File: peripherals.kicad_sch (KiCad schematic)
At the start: 25 parts, among them J10 0533980471, J14 SM04B-SRSS-TB-LF-SN, J7 200528-0100, J8 200528-0100, U33 NTS0102, U35 AP22653, U9 SN74AXC4T774

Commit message: v2.0 Schematic updates
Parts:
- removed C108: 100nF, Capacitor_SMD:C_0603_1608Metric, symbol Device:C_Small
- removed D17, D18: TPD1E0B04, Diode_SMD:D_SOD-882, symbol Device:D_TVS_Small
- removed J14: SM04B-SRSS-TB-LF-SN, JetsonCarrier:Conn_JST_SH_1x4_SM04B-SRSS-TB-LF-SN, symbol JetsonCarrier:JST_SH_1x4_SM04B-SRSS-TB-LF-SN
- removed R145: 10k, Resistor_SMD:R_0603_1608Metric, symbol Device:R_Small
- removed R146: 100k, Resistor_SMD:R_0603_1608Metric, symbol Device:R_Small
- removed R147: 15k, Resistor_SMD:R_0603_1608Metric, symbol Device:R_Small
- removed RN3: 4x0R, Resistor_SMD:R_Array_Concave_4x0402, symbol Device:R_Pack04
- removed TP2, TP3: TP_0.75mm_SMD, JetsonCarrier:TP_SMD_0.75mm, symbol Connector:TestPoint
- removed U35: AP22653, JetsonCarrier:DFN-6-1EP_2x2mm_P0.65mm_EP1x1.6mm, symbol JetsonCarrier:AP22653
- removed U9: SN74AXC4T774, Package_DFN_QFN:UQFN-16_1.8x2.6mm_P0.4mm, symbol JetsonCarrier:SN74AXC4T774
- added U9: NTS0102, JetsonCarrier:XSON-8_1x1.95mm_P0.5mm, symbol JetsonCarrier:NTS0102
- C40, C41: Dielectric (none) -> X5R; MPN C1005X6S1A105K050BC -> GRM155R61H104KE14D; Manufacturer TDK -> Murata; Voltage (none) -> 50V
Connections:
- net MB_CS is gone; now on net GND: J8.6 (Pin_6)
- net MB_MISO is gone; now on net GND: J8.9 (Pin_9)
- net +1V8: now also C40.1, U9.3 (VCC_{A}), U9.6 (OE); no longer C41.1
- net GND: now also C40.2, J8.4 (Pin_4), U9.2 (GND); no longer C40.1, J8.5 (Pin_5)
- net JETSON_EN: now also J8.5 (Pin_5); no longer J8.4 (Pin_4)
- net MB_3V3: now also C41.1, U9.7 (VCC_{B}); no longer C40.2
- net UART1_RXD: now also U9.5 (A_{1})
- net UART1_TXD: now also U9.4 (A_{2})
- net MB_MOSI renamed MB_JETSON_RX
- net MB_JETSON_RX: now also U9.8 (B_{1})
- net MB_SCK renamed MB_JETSON_TX
- net MB_JETSON_TX: now also U9.1 (B_{2})
- no-connect marks 5 -> 0
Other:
- note added: "Mainboard FPC Connector"
- note added: "USB 2.0 FPC Connector"
- note removed: "I2C connector"
- company: Argus-1 Cubesat -> Carnegie Mellon University
- title: Jetson Carrier Board -> Argus Carrierboard
- moved on the sheet: C12, C33, C44, C48, J10, J7, J8, TP29, TP30, TP31, U33

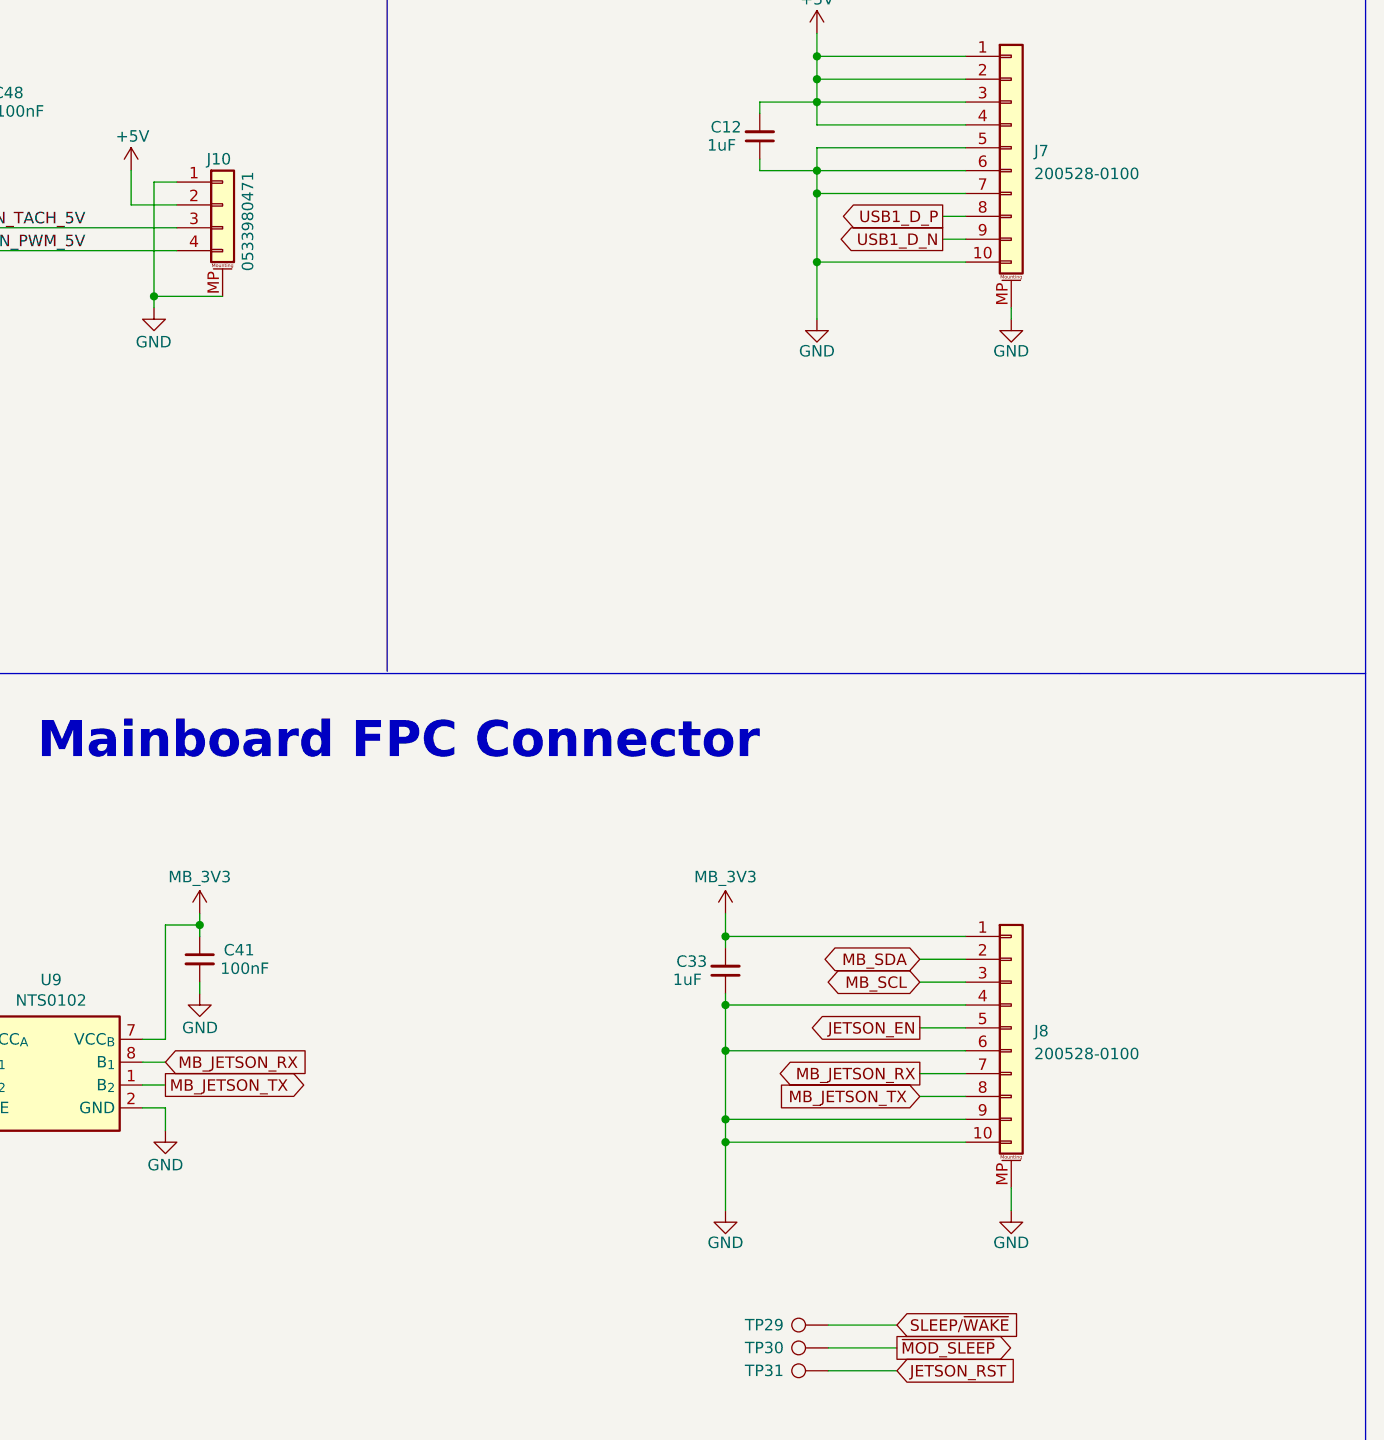
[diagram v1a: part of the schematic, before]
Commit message: v2.0 Layout completed. Exported BOM and STEP files
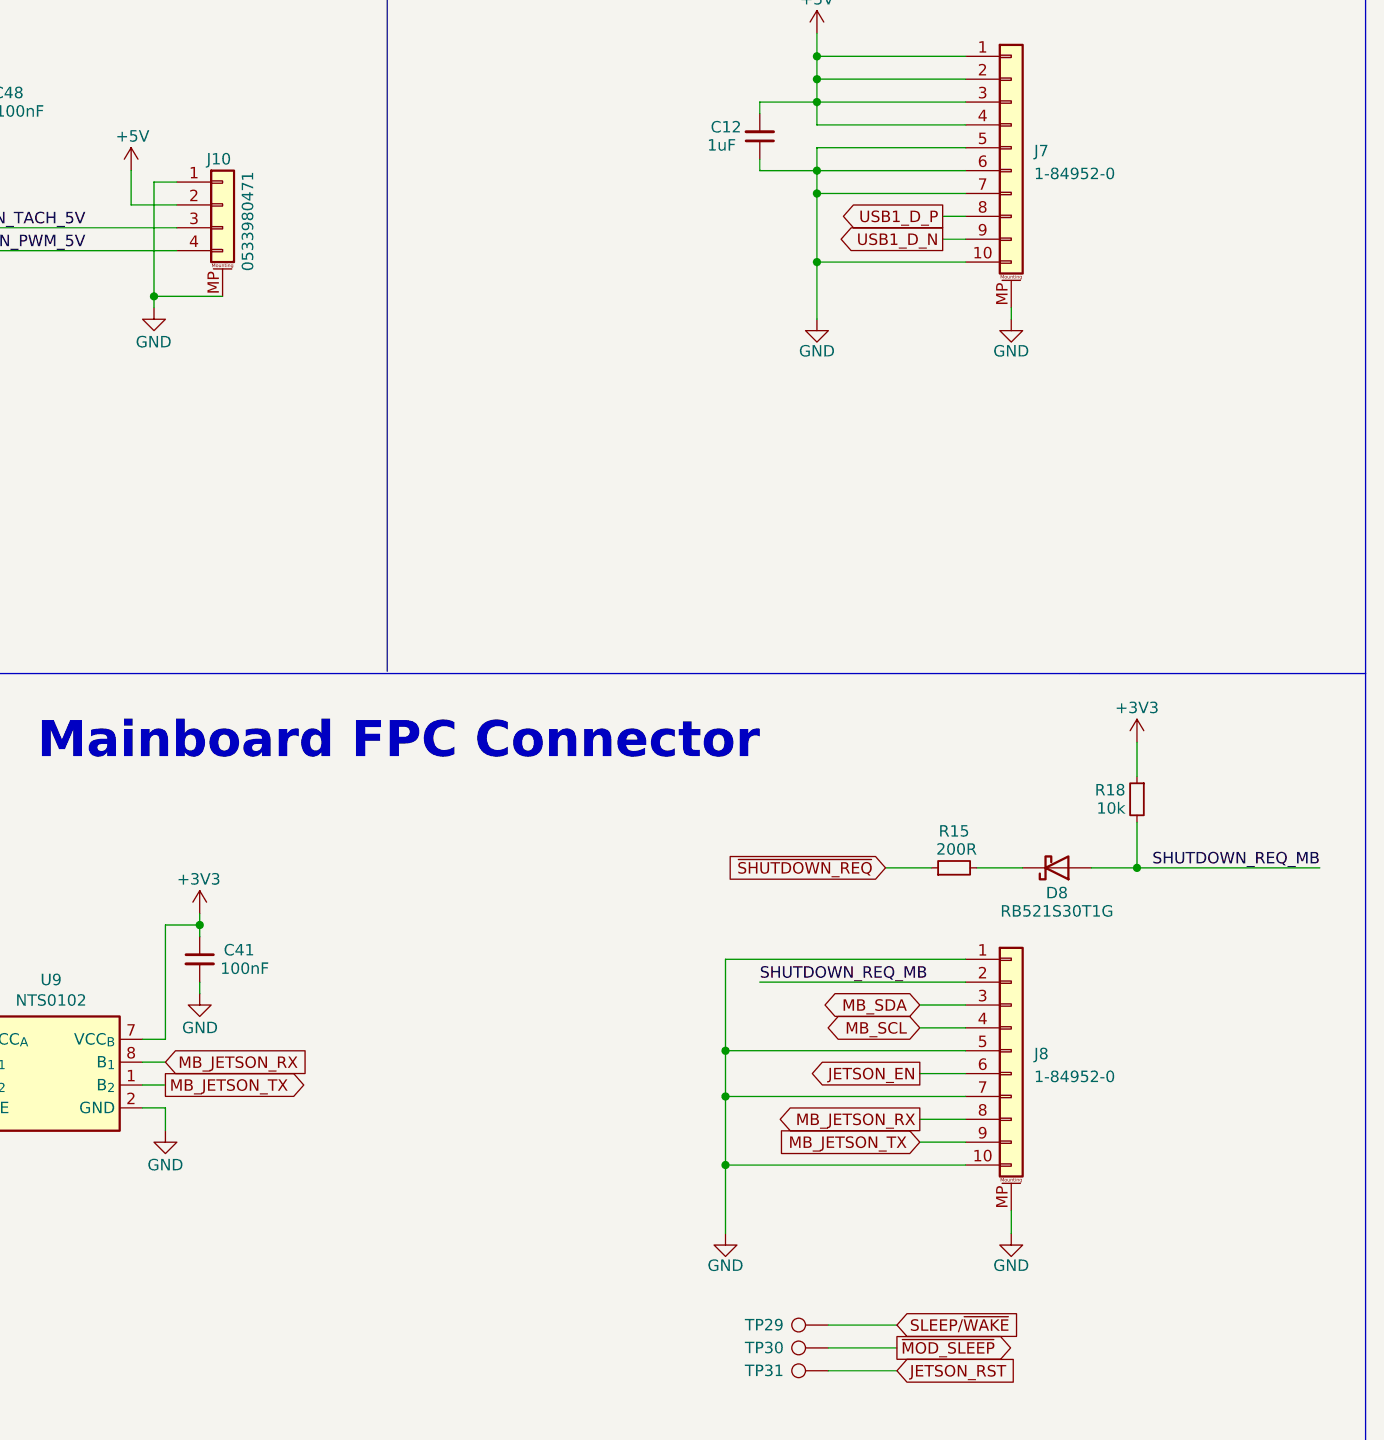
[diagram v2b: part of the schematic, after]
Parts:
- removed C33: 1uF, Capacitor_SMD:C_0603_1608Metric, symbol Device:C_Small
- added D8: RB521S30T1G, Diode_SMD:D_SOD-523, symbol Device:D_Schottky
- added R15: 200R, Resistor_SMD:R_0603_1608Metric, symbol Device:R_Small
- added R18: 10k, Resistor_SMD:R_0603_1608Metric, symbol Device:R_Small
- J7, J8: value 200528-0100 -> 1-84952-0; footprint Connector_FFC-FPC:Molex_200528-0100_1x10-1MP_P1.00mm_Horizontal -> Connector_FFC-FPC:TE_1-84952-0_1x10-1MP_P1.0mm_Horizontal
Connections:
- net GND: now also J8.1 (Pin_1), J8.5 (Pin_5), J8.7 (Pin_7); no longer J8.4 (Pin_4), J8.6 (Pin_6), J8.9 (Pin_9)
- net JETSON_EN: now also J8.6 (Pin_6); no longer J8.5 (Pin_5)
- net MB_JETSON_RX: now also J8.8 (Pin_8); no longer J8.7 (Pin_7)
- net MB_JETSON_TX: now also J8.9 (Pin_9); no longer J8.8 (Pin_8)
- net MB_SCL: now also J8.4 (Pin_4); no longer J8.3 (Pin_3)
- net MB_SDA: now also J8.3 (Pin_3); no longer J8.2 (Pin_2)
- net MB_3V3 renamed +3V3
- net +3V3: now also R18.1; no longer J8.1 (Pin_1)
- new net: D8.1 (K), R15.2
- new net SHUTDOWN_REQ_MB: D8.2 (A), J8.2 (Pin_2), R18.2
- new net ~{SHUTDOWN_REQ}: R15.1
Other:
- moved on the sheet: J8

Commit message: v2.1 Updates
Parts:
- C12: Author Antmicro -> (none); License Apache-2.0 -> (none); MPN C1005X6S1A105K050BC -> C2214844; Manufacturer TDK -> (none); Val 1u -> (none)
- C40, C41, C44, C48: Author Antmicro -> (none); Dielectric X5R -> (none); License Apache-2.0 -> (none); MPN GRM155R61H104KE14D -> C307348; Val 100n -> (none); Voltage 50V -> (none)
- J10: Author Antmicro -> (none); License Apache-2.0 -> (none); MPN 0533980471 -> C225106; Manufacturer Molex -> (none)
- J7, J8: value 1-84952-0 -> 522711069; footprint Connector_FFC-FPC:TE_1-84952-0_1x10-1MP_P1.0mm_Horizontal -> JetsonCarrier:CON_522711069_MOL; MPN (none) -> C588180
- R15: footprint Resistor_SMD:R_0603_1608Metric -> Resistor_SMD:R_0402_1005Metric; Author Antmicro -> (none); License Apache-2.0 -> (none); MPN CR0402-FX-2000GLF -> C413070; Manufacturer Bourns -> (none); Tolerance 1% -> (none); Val 200R -> (none)
- R18: footprint Resistor_SMD:R_0603_1608Metric -> Resistor_SMD:R_0402_1005Metric; MPN (none) -> C71617
- TP29, TP30, TP31: now left out of the parts list
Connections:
- net +3V3: no longer R18.1
- new net 3V3_STDB: R18.1
